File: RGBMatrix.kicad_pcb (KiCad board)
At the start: 2 copper layers, 208 parts

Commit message: anodColumn, colorRow
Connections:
- LED10 pad 1: B10 -> B01
- LED10 pad 2: G10 -> G01
- LED10 pad 3: R10 -> R01
- LED10 pad 4: A01 -> A10
- LED100 pad 1: B04 -> B07
- LED100 pad 2: G04 -> G07
- LED100 pad 3: R04 -> R07
- LED100 pad 4: A07 -> A04
- LED101 pad 1: B05 -> B07
- LED101 pad 2: G05 -> G07
- LED101 pad 3: R05 -> R07
- LED101 pad 4: A07 -> A05
- LED102 pad 1: B06 -> B07
- LED102 pad 2: G06 -> G07
- LED102 pad 3: R06 -> R07
- LED102 pad 4: A07 -> A06
- LED104 pad 1: B08 -> B07
- LED104 pad 2: G08 -> G07
- LED104 pad 3: R08 -> R07
- LED104 pad 4: A07 -> A08
- LED105 pad 1: B09 -> B07
- LED105 pad 2: G09 -> G07
- LED105 pad 3: R09 -> R07
- LED105 pad 4: A07 -> A09
- LED106 pad 1: B10 -> B07
- LED106 pad 2: G10 -> G07
- LED106 pad 3: R10 -> R07
- LED106 pad 4: A07 -> A10
- LED107 pad 1: B11 -> B07
- LED107 pad 2: G11 -> G07
- LED107 pad 3: R11 -> R07
- LED107 pad 4: A07 -> A11
- LED108 pad 1: B12 -> B07
- LED108 pad 2: G12 -> G07
- LED108 pad 3: R12 -> R07
- LED108 pad 4: A07 -> A12
- LED109 pad 1: B13 -> B07
- LED109 pad 2: G13 -> G07
- LED109 pad 3: R13 -> R07
- LED109 pad 4: A07 -> A13
- LED11 pad 1: B11 -> B01
- LED11 pad 2: G11 -> G01
- LED11 pad 3: R11 -> R01
- LED11 pad 4: A01 -> A11
- LED110 pad 1: B14 -> B07
- LED110 pad 2: G14 -> G07
- LED110 pad 3: R14 -> R07
- LED110 pad 4: A07 -> A14
- LED111 pad 1: B15 -> B07
- LED111 pad 2: G15 -> G07
- LED111 pad 3: R15 -> R07
- LED111 pad 4: A07 -> A15
- LED112 pad 1: B16 -> B07
- LED112 pad 2: G16 -> G07
- LED112 pad 3: R16 -> R07
- LED112 pad 4: A07 -> A16
- LED113 pad 1: B01 -> B08
- LED113 pad 2: G01 -> G08
- LED113 pad 3: R01 -> R08
- LED113 pad 4: A08 -> A01
- LED114 pad 1: B02 -> B08
- LED114 pad 2: G02 -> G08
- LED114 pad 3: R02 -> R08
- LED114 pad 4: A08 -> A02
- LED115 pad 1: B03 -> B08
- LED115 pad 2: G03 -> G08
- LED115 pad 3: R03 -> R08
- LED115 pad 4: A08 -> A03
- LED116 pad 1: B04 -> B08
- LED116 pad 2: G04 -> G08
- LED116 pad 3: R04 -> R08
- LED116 pad 4: A08 -> A04
- LED117 pad 1: B05 -> B08
- LED117 pad 2: G05 -> G08
- LED117 pad 3: R05 -> R08
- LED117 pad 4: A08 -> A05
- LED118 pad 1: B06 -> B08
- LED118 pad 2: G06 -> G08
- LED118 pad 3: R06 -> R08
- LED118 pad 4: A08 -> A06
- LED119 pad 1: B07 -> B08
- LED119 pad 2: G07 -> G08
- LED119 pad 3: R07 -> R08
- LED119 pad 4: A08 -> A07
- LED12 pad 1: B12 -> B01
- LED12 pad 2: G12 -> G01
- LED12 pad 3: R12 -> R01
- LED12 pad 4: A01 -> A12
- LED121 pad 1: B09 -> B08
- LED121 pad 2: G09 -> G08
- LED121 pad 3: R09 -> R08
- LED121 pad 4: A08 -> A09
- LED122 pad 1: B10 -> B08
- LED122 pad 2: G10 -> G08
- LED122 pad 3: R10 -> R08
- LED122 pad 4: A08 -> A10
- LED123 pad 1: B11 -> B08
- LED123 pad 2: G11 -> G08
- LED123 pad 3: R11 -> R08
- LED123 pad 4: A08 -> A11
- LED124 pad 1: B12 -> B08
- LED124 pad 2: G12 -> G08
- LED124 pad 3: R12 -> R08
- LED124 pad 4: A08 -> A12
- LED125 pad 1: B13 -> B08
- LED125 pad 2: G13 -> G08
- LED125 pad 3: R13 -> R08
- LED125 pad 4: A08 -> A13
- LED126 pad 1: B14 -> B08
- LED126 pad 2: G14 -> G08
- LED126 pad 3: R14 -> R08
- LED126 pad 4: A08 -> A14
- LED127 pad 1: B15 -> B08
- LED127 pad 2: G15 -> G08
- LED127 pad 3: R15 -> R08
- LED127 pad 4: A08 -> A15
- LED128 pad 1: B16 -> B08
- LED128 pad 2: G16 -> G08
- LED128 pad 3: R16 -> R08
- LED128 pad 4: A08 -> A16
- LED129 pad 1: B01 -> B09
- LED129 pad 2: G01 -> G09
- LED129 pad 3: R01 -> R09
- LED129 pad 4: A09 -> A01
- LED13 pad 1: B13 -> B01
- LED13 pad 2: G13 -> G01
- LED13 pad 3: R13 -> R01
- LED13 pad 4: A01 -> A13
- LED130 pad 1: B02 -> B09
- LED130 pad 2: G02 -> G09
- LED130 pad 3: R02 -> R09
- LED130 pad 4: A09 -> A02
- LED131 pad 1: B03 -> B09
- LED131 pad 2: G03 -> G09
- LED131 pad 3: R03 -> R09
- LED131 pad 4: A09 -> A03
- LED132 pad 1: B04 -> B09
- LED132 pad 2: G04 -> G09
- LED132 pad 3: R04 -> R09
- LED132 pad 4: A09 -> A04
- LED133 pad 1: B05 -> B09
- LED133 pad 2: G05 -> G09
- LED133 pad 3: R05 -> R09
- LED133 pad 4: A09 -> A05
- LED134 pad 1: B06 -> B09
- LED134 pad 2: G06 -> G09
- LED134 pad 3: R06 -> R09
- LED134 pad 4: A09 -> A06
- LED135 pad 1: B07 -> B09
- LED135 pad 2: G07 -> G09
- LED135 pad 3: R07 -> R09
- LED135 pad 4: A09 -> A07
- LED136 pad 1: B08 -> B09
- LED136 pad 2: G08 -> G09
- LED136 pad 3: R08 -> R09
- LED136 pad 4: A09 -> A08
- LED138 pad 1: B10 -> B09
- LED138 pad 2: G10 -> G09
- LED138 pad 3: R10 -> R09
- LED138 pad 4: A09 -> A10
- LED139 pad 1: B11 -> B09
- LED139 pad 2: G11 -> G09
- LED139 pad 3: R11 -> R09
- LED139 pad 4: A09 -> A11
- LED14 pad 1: B14 -> B01
- LED14 pad 2: G14 -> G01
- LED14 pad 3: R14 -> R01
- LED14 pad 4: A01 -> A14
- LED140 pad 1: B12 -> B09
- LED140 pad 2: G12 -> G09
- LED140 pad 3: R12 -> R09
- LED140 pad 4: A09 -> A12
- LED141 pad 1: B13 -> B09
- LED141 pad 2: G13 -> G09
- LED141 pad 3: R13 -> R09
- LED141 pad 4: A09 -> A13
- LED142 pad 1: B14 -> B09
- LED142 pad 2: G14 -> G09
- LED142 pad 3: R14 -> R09
- LED142 pad 4: A09 -> A14
- LED143 pad 1: B15 -> B09
- LED143 pad 2: G15 -> G09
- LED143 pad 3: R15 -> R09
- LED143 pad 4: A09 -> A15
- LED144 pad 1: B16 -> B09
- LED144 pad 2: G16 -> G09
- LED144 pad 3: R16 -> R09
- LED144 pad 4: A09 -> A16
- LED145 pad 1: B01 -> B10
- LED145 pad 2: G01 -> G10
- LED145 pad 3: R01 -> R10
- LED145 pad 4: A10 -> A01
- LED146 pad 1: B02 -> B10
- LED146 pad 2: G02 -> G10
- LED146 pad 3: R02 -> R10
- LED146 pad 4: A10 -> A02
- LED147 pad 1: B03 -> B10
- LED147 pad 2: G03 -> G10
- LED147 pad 3: R03 -> R10
- LED147 pad 4: A10 -> A03
- LED148 pad 1: B04 -> B10
- LED148 pad 2: G04 -> G10
- LED148 pad 3: R04 -> R10
- LED148 pad 4: A10 -> A04
- LED149 pad 1: B05 -> B10
- LED149 pad 2: G05 -> G10
- LED149 pad 3: R05 -> R10
- LED149 pad 4: A10 -> A05
- LED15 pad 1: B15 -> B01
- LED15 pad 2: G15 -> G01
- LED15 pad 3: R15 -> R01
- LED15 pad 4: A01 -> A15
- LED150 pad 1: B06 -> B10
- LED150 pad 2: G06 -> G10
- LED150 pad 3: R06 -> R10
- LED150 pad 4: A10 -> A06
- LED151 pad 1: B07 -> B10
- LED151 pad 2: G07 -> G10
- LED151 pad 3: R07 -> R10
- LED151 pad 4: A10 -> A07
- LED152 pad 1: B08 -> B10
- LED152 pad 2: G08 -> G10
- LED152 pad 3: R08 -> R10
- LED152 pad 4: A10 -> A08
- LED153 pad 1: B09 -> B10
- LED153 pad 2: G09 -> G10
- LED153 pad 3: R09 -> R10
- LED153 pad 4: A10 -> A09
- LED155 pad 1: B11 -> B10
- LED155 pad 2: G11 -> G10
- LED155 pad 3: R11 -> R10
- LED155 pad 4: A10 -> A11
- LED156 pad 1: B12 -> B10
- LED156 pad 2: G12 -> G10
- LED156 pad 3: R12 -> R10
- LED156 pad 4: A10 -> A12
- LED157 pad 1: B13 -> B10
- LED157 pad 2: G13 -> G10
- LED157 pad 3: R13 -> R10
- LED157 pad 4: A10 -> A13
- LED158 pad 1: B14 -> B10
- LED158 pad 2: G14 -> G10
- LED158 pad 3: R14 -> R10
- LED158 pad 4: A10 -> A14
- LED159 pad 1: B15 -> B10
- LED159 pad 2: G15 -> G10
- LED159 pad 3: R15 -> R10
- LED159 pad 4: A10 -> A15
- LED16 pad 1: B16 -> B01
- LED16 pad 2: G16 -> G01
- LED16 pad 3: R16 -> R01
- LED16 pad 4: A01 -> A16
- LED160 pad 1: B16 -> B10
- LED160 pad 2: G16 -> G10
- LED160 pad 3: R16 -> R10
- LED160 pad 4: A10 -> A16
- LED161 pad 1: B01 -> B11
- LED161 pad 2: G01 -> G11
- LED161 pad 3: R01 -> R11
- LED161 pad 4: A11 -> A01
- LED162 pad 1: B02 -> B11
- LED162 pad 2: G02 -> G11
- LED162 pad 3: R02 -> R11
- LED162 pad 4: A11 -> A02
- LED163 pad 1: B03 -> B11
- LED163 pad 2: G03 -> G11
- LED163 pad 3: R03 -> R11
- LED163 pad 4: A11 -> A03
- LED164 pad 1: B04 -> B11
- LED164 pad 2: G04 -> G11
- LED164 pad 3: R04 -> R11
- LED164 pad 4: A11 -> A04
- LED165 pad 1: B05 -> B11
- LED165 pad 2: G05 -> G11
- LED165 pad 3: R05 -> R11
- LED165 pad 4: A11 -> A05
- LED166 pad 1: B06 -> B11
- LED166 pad 2: G06 -> G11
- LED166 pad 3: R06 -> R11
- LED166 pad 4: A11 -> A06
- LED167 pad 1: B07 -> B11
- LED167 pad 2: G07 -> G11
- LED167 pad 3: R07 -> R11
- LED167 pad 4: A11 -> A07
- LED168 pad 1: B08 -> B11
- LED168 pad 2: G08 -> G11
- LED168 pad 3: R08 -> R11
- LED168 pad 4: A11 -> A08
- LED169 pad 1: B09 -> B11
- LED169 pad 2: G09 -> G11
- LED169 pad 3: R09 -> R11
- LED169 pad 4: A11 -> A09
- LED17 pad 1: B01 -> B02
- LED17 pad 2: G01 -> G02
- LED17 pad 3: R01 -> R02
- LED17 pad 4: A02 -> A01
- LED170 pad 1: B10 -> B11
- LED170 pad 2: G10 -> G11
- LED170 pad 3: R10 -> R11
- LED170 pad 4: A11 -> A10
- LED172 pad 1: B12 -> B11
- LED172 pad 2: G12 -> G11
- LED172 pad 3: R12 -> R11
- LED172 pad 4: A11 -> A12
- LED173 pad 1: B13 -> B11
- LED173 pad 2: G13 -> G11
- LED173 pad 3: R13 -> R11
- LED173 pad 4: A11 -> A13
- LED174 pad 1: B14 -> B11
- LED174 pad 2: G14 -> G11
- LED174 pad 3: R14 -> R11
- LED174 pad 4: A11 -> A14
- LED175 pad 1: B15 -> B11
- LED175 pad 2: G15 -> G11
- LED175 pad 3: R15 -> R11
- LED175 pad 4: A11 -> A15
- LED176 pad 1: B16 -> B11
- LED176 pad 2: G16 -> G11
- LED176 pad 3: R16 -> R11
- LED176 pad 4: A11 -> A16
- LED177 pad 1: B01 -> B12
- LED177 pad 2: G01 -> G12
- LED177 pad 3: R01 -> R12
- LED177 pad 4: A12 -> A01
- LED178 pad 1: B02 -> B12
- LED178 pad 2: G02 -> G12
- LED178 pad 3: R02 -> R12
- LED178 pad 4: A12 -> A02
- LED179 pad 1: B03 -> B12
- LED179 pad 2: G03 -> G12
- LED179 pad 3: R03 -> R12
- LED179 pad 4: A12 -> A03
- LED180 pad 1: B04 -> B12
- LED180 pad 2: G04 -> G12
- LED180 pad 3: R04 -> R12
- LED180 pad 4: A12 -> A04
- LED181 pad 1: B05 -> B12
- LED181 pad 2: G05 -> G12
- LED181 pad 3: R05 -> R12
- LED181 pad 4: A12 -> A05
- LED182 pad 1: B06 -> B12
- LED182 pad 2: G06 -> G12
- LED182 pad 3: R06 -> R12
- LED182 pad 4: A12 -> A06
- LED183 pad 1: B07 -> B12
- LED183 pad 2: G07 -> G12
- LED183 pad 3: R07 -> R12
- LED183 pad 4: A12 -> A07
- LED184 pad 1: B08 -> B12
- LED184 pad 2: G08 -> G12
- LED184 pad 3: R08 -> R12
- LED184 pad 4: A12 -> A08
- LED185 pad 1: B09 -> B12
- LED185 pad 2: G09 -> G12
- LED185 pad 3: R09 -> R12
- LED185 pad 4: A12 -> A09
- LED186 pad 1: B10 -> B12
- LED186 pad 2: G10 -> G12
- LED186 pad 3: R10 -> R12
- LED186 pad 4: A12 -> A10
- LED187 pad 1: B11 -> B12
- LED187 pad 2: G11 -> G12
- LED187 pad 3: R11 -> R12
- LED187 pad 4: A12 -> A11
- LED189 pad 1: B13 -> B12
- LED189 pad 2: G13 -> G12
- LED189 pad 3: R13 -> R12
- LED189 pad 4: A12 -> A13
- LED19 pad 1: B03 -> B02
- LED19 pad 2: G03 -> G02
- LED19 pad 3: R03 -> R02
- LED19 pad 4: A02 -> A03
- LED190 pad 1: B14 -> B12
- LED190 pad 2: G14 -> G12
- LED190 pad 3: R14 -> R12
- LED190 pad 4: A12 -> A14
- LED191 pad 1: B15 -> B12
- LED191 pad 2: G15 -> G12
- LED191 pad 3: R15 -> R12
- LED191 pad 4: A12 -> A15
- LED192 pad 1: B16 -> B12
- LED192 pad 2: G16 -> G12
- LED192 pad 3: R16 -> R12
- LED192 pad 4: A12 -> A16
- LED193 pad 1: B01 -> B13
- LED193 pad 2: G01 -> G13
- LED193 pad 3: R01 -> R13
- LED193 pad 4: A13 -> A01
- LED194 pad 1: B02 -> B13
- LED194 pad 2: G02 -> G13
- LED194 pad 3: R02 -> R13
- LED194 pad 4: A13 -> A02
- LED195 pad 1: B03 -> B13
- LED195 pad 2: G03 -> G13
- LED195 pad 3: R03 -> R13
- LED195 pad 4: A13 -> A03
- LED196 pad 1: B04 -> B13
- LED196 pad 2: G04 -> G13
- LED196 pad 3: R04 -> R13
- LED196 pad 4: A13 -> A04
- LED197 pad 1: B05 -> B13
- LED197 pad 2: G05 -> G13
- LED197 pad 3: R05 -> R13
- LED197 pad 4: A13 -> A05
- LED198 pad 1: B06 -> B13
- LED198 pad 2: G06 -> G13
- LED198 pad 3: R06 -> R13
- LED198 pad 4: A13 -> A06
- LED199 pad 1: B07 -> B13
- LED199 pad 2: G07 -> G13
- LED199 pad 3: R07 -> R13
- LED199 pad 4: A13 -> A07
- LED2 pad 1: B02 -> B01
- LED2 pad 2: G02 -> G01
- LED2 pad 3: R02 -> R01
- LED2 pad 4: A01 -> A02
- LED20 pad 1: B04 -> B02
- LED20 pad 2: G04 -> G02
- LED20 pad 3: R04 -> R02
- LED20 pad 4: A02 -> A04
- LED200 pad 1: B08 -> B13
- LED200 pad 2: G08 -> G13
- LED200 pad 3: R08 -> R13
- LED200 pad 4: A13 -> A08
- LED201 pad 1: B09 -> B13
- LED201 pad 2: G09 -> G13
- LED201 pad 3: R09 -> R13
- LED201 pad 4: A13 -> A09
- LED202 pad 1: B10 -> B13
- LED202 pad 2: G10 -> G13
- LED202 pad 3: R10 -> R13
- LED202 pad 4: A13 -> A10
- LED203 pad 1: B11 -> B13
- LED203 pad 2: G11 -> G13
- LED203 pad 3: R11 -> R13
- LED203 pad 4: A13 -> A11
- LED204 pad 1: B12 -> B13
- LED204 pad 2: G12 -> G13
- LED204 pad 3: R12 -> R13
- LED204 pad 4: A13 -> A12
- LED206 pad 1: B14 -> B13
- LED206 pad 2: G14 -> G13
- LED206 pad 3: R14 -> R13
- LED206 pad 4: A13 -> A14
- LED207 pad 1: B15 -> B13
- LED207 pad 2: G15 -> G13
- LED207 pad 3: R15 -> R13
- LED207 pad 4: A13 -> A15
- LED208 pad 1: B16 -> B13
- LED208 pad 2: G16 -> G13
- LED208 pad 3: R16 -> R13
- LED208 pad 4: A13 -> A16
- LED21 pad 1: B05 -> B02
- LED21 pad 2: G05 -> G02
- LED21 pad 3: R05 -> R02
- LED21 pad 4: A02 -> A05
- LED22 pad 1: B06 -> B02
- LED22 pad 2: G06 -> G02
- LED22 pad 3: R06 -> R02
- LED22 pad 4: A02 -> A06
- LED23 pad 1: B07 -> B02
- LED23 pad 2: G07 -> G02
- LED23 pad 3: R07 -> R02
- LED23 pad 4: A02 -> A07
- LED24 pad 1: B08 -> B02
- LED24 pad 2: G08 -> G02
- LED24 pad 3: R08 -> R02
- LED24 pad 4: A02 -> A08
- LED25 pad 1: B09 -> B02
- LED25 pad 2: G09 -> G02
- LED25 pad 3: R09 -> R02
- LED25 pad 4: A02 -> A09
- LED26 pad 1: B10 -> B02
- LED26 pad 2: G10 -> G02
- LED26 pad 3: R10 -> R02
- LED26 pad 4: A02 -> A10
- LED27 pad 1: B11 -> B02
- LED27 pad 2: G11 -> G02
- LED27 pad 3: R11 -> R02
- LED27 pad 4: A02 -> A11
- LED28 pad 1: B12 -> B02
- LED28 pad 2: G12 -> G02
- LED28 pad 3: R12 -> R02
- LED28 pad 4: A02 -> A12
- LED29 pad 1: B13 -> B02
- LED29 pad 2: G13 -> G02
- LED29 pad 3: R13 -> R02
- LED29 pad 4: A02 -> A13
- LED3 pad 1: B03 -> B01
- LED3 pad 2: G03 -> G01
- LED3 pad 3: R03 -> R01
- LED3 pad 4: A01 -> A03
- LED30 pad 1: B14 -> B02
- LED30 pad 2: G14 -> G02
- LED30 pad 3: R14 -> R02
- LED30 pad 4: A02 -> A14
- LED31 pad 1: B15 -> B02
- LED31 pad 2: G15 -> G02
- LED31 pad 3: R15 -> R02
- LED31 pad 4: A02 -> A15
- LED32 pad 1: B16 -> B02
- LED32 pad 2: G16 -> G02
- LED32 pad 3: R16 -> R02
- LED32 pad 4: A02 -> A16
- LED33 pad 1: B01 -> B03
- LED33 pad 2: G01 -> G03
- LED33 pad 3: R01 -> R03
- LED33 pad 4: A03 -> A01
- LED34 pad 1: B02 -> B03
- LED34 pad 2: G02 -> G03
- LED34 pad 3: R02 -> R03
- LED34 pad 4: A03 -> A02
- LED36 pad 1: B04 -> B03
- LED36 pad 2: G04 -> G03
- LED36 pad 3: R04 -> R03
- LED36 pad 4: A03 -> A04
- LED37 pad 1: B05 -> B03
- LED37 pad 2: G05 -> G03
- LED37 pad 3: R05 -> R03
- LED37 pad 4: A03 -> A05
- LED38 pad 1: B06 -> B03
- LED38 pad 2: G06 -> G03
- LED38 pad 3: R06 -> R03
- LED38 pad 4: A03 -> A06
- LED39 pad 1: B07 -> B03
- LED39 pad 2: G07 -> G03
- LED39 pad 3: R07 -> R03
- LED39 pad 4: A03 -> A07
- LED4 pad 1: B04 -> B01
- LED4 pad 2: G04 -> G01
- LED4 pad 3: R04 -> R01
- LED4 pad 4: A01 -> A04
- LED40 pad 1: B08 -> B03
- LED40 pad 2: G08 -> G03
- LED40 pad 3: R08 -> R03
- LED40 pad 4: A03 -> A08
- LED41 pad 1: B09 -> B03
- LED41 pad 2: G09 -> G03
- LED41 pad 3: R09 -> R03
- LED41 pad 4: A03 -> A09
- LED42 pad 1: B10 -> B03
- LED42 pad 2: G10 -> G03
- LED42 pad 3: R10 -> R03
- LED42 pad 4: A03 -> A10
- LED43 pad 1: B11 -> B03
- LED43 pad 2: G11 -> G03
- LED43 pad 3: R11 -> R03
- LED43 pad 4: A03 -> A11
- LED44 pad 1: B12 -> B03
- LED44 pad 2: G12 -> G03
- LED44 pad 3: R12 -> R03
- LED44 pad 4: A03 -> A12
- LED45 pad 1: B13 -> B03
- LED45 pad 2: G13 -> G03
- LED45 pad 3: R13 -> R03
- LED45 pad 4: A03 -> A13
- LED46 pad 1: B14 -> B03
- LED46 pad 2: G14 -> G03
- LED46 pad 3: R14 -> R03
- LED46 pad 4: A03 -> A14
- LED47 pad 1: B15 -> B03
- LED47 pad 2: G15 -> G03
- LED47 pad 3: R15 -> R03
- LED47 pad 4: A03 -> A15
- LED48 pad 1: B16 -> B03
- LED48 pad 2: G16 -> G03
- LED48 pad 3: R16 -> R03
- LED48 pad 4: A03 -> A16
- LED49 pad 1: B01 -> B04
- LED49 pad 2: G01 -> G04
- LED49 pad 3: R01 -> R04
- LED49 pad 4: A04 -> A01
- LED5 pad 1: B05 -> B01
- LED5 pad 2: G05 -> G01
- LED5 pad 3: R05 -> R01
- LED5 pad 4: A01 -> A05
- LED50 pad 1: B02 -> B04
- LED50 pad 2: G02 -> G04
- LED50 pad 3: R02 -> R04
- LED50 pad 4: A04 -> A02
- LED51 pad 1: B03 -> B04
- LED51 pad 2: G03 -> G04
- LED51 pad 3: R03 -> R04
- LED51 pad 4: A04 -> A03
- LED53 pad 1: B05 -> B04
- LED53 pad 2: G05 -> G04
- LED53 pad 3: R05 -> R04
- LED53 pad 4: A04 -> A05
- LED54 pad 1: B06 -> B04
- LED54 pad 2: G06 -> G04
- LED54 pad 3: R06 -> R04
- LED54 pad 4: A04 -> A06
- LED55 pad 1: B07 -> B04
- LED55 pad 2: G07 -> G04
- LED55 pad 3: R07 -> R04
- LED55 pad 4: A04 -> A07
- LED56 pad 1: B08 -> B04
- LED56 pad 2: G08 -> G04
- LED56 pad 3: R08 -> R04
- LED56 pad 4: A04 -> A08
- LED57 pad 1: B09 -> B04
- LED57 pad 2: G09 -> G04
- LED57 pad 3: R09 -> R04
- LED57 pad 4: A04 -> A09
- LED58 pad 1: B10 -> B04
- LED58 pad 2: G10 -> G04
- LED58 pad 3: R10 -> R04
- LED58 pad 4: A04 -> A10
- LED59 pad 1: B11 -> B04
- LED59 pad 2: G11 -> G04
- LED59 pad 3: R11 -> R04
- LED59 pad 4: A04 -> A11
- LED6 pad 1: B06 -> B01
- LED6 pad 2: G06 -> G01
- LED6 pad 3: R06 -> R01
- LED6 pad 4: A01 -> A06
- LED60 pad 1: B12 -> B04
- LED60 pad 2: G12 -> G04
- LED60 pad 3: R12 -> R04
- LED60 pad 4: A04 -> A12
- LED61 pad 1: B13 -> B04
- LED61 pad 2: G13 -> G04
- LED61 pad 3: R13 -> R04
- LED61 pad 4: A04 -> A13
- LED62 pad 1: B14 -> B04
- LED62 pad 2: G14 -> G04
- LED62 pad 3: R14 -> R04
- LED62 pad 4: A04 -> A14
- LED63 pad 1: B15 -> B04
- LED63 pad 2: G15 -> G04
- LED63 pad 3: R15 -> R04
- LED63 pad 4: A04 -> A15
- LED64 pad 1: B16 -> B04
- LED64 pad 2: G16 -> G04
- LED64 pad 3: R16 -> R04
- LED64 pad 4: A04 -> A16
- LED65 pad 1: B01 -> B05
- LED65 pad 2: G01 -> G05
- LED65 pad 3: R01 -> R05
- LED65 pad 4: A05 -> A01
- LED66 pad 1: B02 -> B05
- LED66 pad 2: G02 -> G05
- LED66 pad 3: R02 -> R05
- LED66 pad 4: A05 -> A02
- LED67 pad 1: B03 -> B05
- LED67 pad 2: G03 -> G05
- LED67 pad 3: R03 -> R05
- LED67 pad 4: A05 -> A03
- LED68 pad 1: B04 -> B05
- LED68 pad 2: G04 -> G05
- LED68 pad 3: R04 -> R05
- LED68 pad 4: A05 -> A04
- LED7 pad 1: B07 -> B01
- LED7 pad 2: G07 -> G01
- LED7 pad 3: R07 -> R01
- LED7 pad 4: A01 -> A07
- LED70 pad 1: B06 -> B05
- LED70 pad 2: G06 -> G05
- LED70 pad 3: R06 -> R05
- LED70 pad 4: A05 -> A06
- LED71 pad 1: B07 -> B05
- LED71 pad 2: G07 -> G05
- LED71 pad 3: R07 -> R05
- LED71 pad 4: A05 -> A07
- LED72 pad 1: B08 -> B05
- LED72 pad 2: G08 -> G05
- LED72 pad 3: R08 -> R05
- LED72 pad 4: A05 -> A08
- LED73 pad 1: B09 -> B05
- LED73 pad 2: G09 -> G05
- LED73 pad 3: R09 -> R05
- LED73 pad 4: A05 -> A09
- LED74 pad 1: B10 -> B05
- LED74 pad 2: G10 -> G05
- LED74 pad 3: R10 -> R05
- LED74 pad 4: A05 -> A10
- LED75 pad 1: B11 -> B05
- LED75 pad 2: G11 -> G05
- LED75 pad 3: R11 -> R05
- LED75 pad 4: A05 -> A11
- LED76 pad 1: B12 -> B05
- LED76 pad 2: G12 -> G05
- LED76 pad 3: R12 -> R05
- LED76 pad 4: A05 -> A12
- LED77 pad 1: B13 -> B05
- LED77 pad 2: G13 -> G05
- LED77 pad 3: R13 -> R05
- LED77 pad 4: A05 -> A13
- LED78 pad 1: B14 -> B05
- LED78 pad 2: G14 -> G05
- LED78 pad 3: R14 -> R05
- LED78 pad 4: A05 -> A14
- LED79 pad 1: B15 -> B05
- LED79 pad 2: G15 -> G05
- LED79 pad 3: R15 -> R05
- LED79 pad 4: A05 -> A15
- LED8 pad 1: B08 -> B01
- LED8 pad 2: G08 -> G01
- LED8 pad 3: R08 -> R01
- LED8 pad 4: A01 -> A08
- LED80 pad 1: B16 -> B05
- LED80 pad 2: G16 -> G05
- LED80 pad 3: R16 -> R05
- LED80 pad 4: A05 -> A16
- LED81 pad 1: B01 -> B06
- LED81 pad 2: G01 -> G06
- LED81 pad 3: R01 -> R06
- LED81 pad 4: A06 -> A01
- LED82 pad 1: B02 -> B06
- LED82 pad 2: G02 -> G06
- LED82 pad 3: R02 -> R06
- LED82 pad 4: A06 -> A02
- LED83 pad 1: B03 -> B06
- LED83 pad 2: G03 -> G06
- LED83 pad 3: R03 -> R06
- LED83 pad 4: A06 -> A03
- LED84 pad 1: B04 -> B06
- LED84 pad 2: G04 -> G06
- LED84 pad 3: R04 -> R06
- LED84 pad 4: A06 -> A04
- LED85 pad 1: B05 -> B06
- LED85 pad 2: G05 -> G06
- LED85 pad 3: R05 -> R06
- LED85 pad 4: A06 -> A05
- LED87 pad 1: B07 -> B06
- LED87 pad 2: G07 -> G06
- LED87 pad 3: R07 -> R06
- LED87 pad 4: A06 -> A07
- LED88 pad 1: B08 -> B06
- LED88 pad 2: G08 -> G06
- LED88 pad 3: R08 -> R06
- LED88 pad 4: A06 -> A08
- LED89 pad 1: B09 -> B06
- LED89 pad 2: G09 -> G06
- LED89 pad 3: R09 -> R06
- LED89 pad 4: A06 -> A09
- LED9 pad 1: B09 -> B01
- LED9 pad 2: G09 -> G01
- LED9 pad 3: R09 -> R01
- LED9 pad 4: A01 -> A09
- LED90 pad 1: B10 -> B06
- LED90 pad 2: G10 -> G06
- LED90 pad 3: R10 -> R06
- LED90 pad 4: A06 -> A10
- LED91 pad 1: B11 -> B06
- LED91 pad 2: G11 -> G06
- LED91 pad 3: R11 -> R06
- LED91 pad 4: A06 -> A11
- LED92 pad 1: B12 -> B06
- LED92 pad 2: G12 -> G06
- LED92 pad 3: R12 -> R06
- LED92 pad 4: A06 -> A12
- LED93 pad 1: B13 -> B06
- LED93 pad 2: G13 -> G06
- LED93 pad 3: R13 -> R06
- LED93 pad 4: A06 -> A13
- LED94 pad 1: B14 -> B06
- LED94 pad 2: G14 -> G06
- LED94 pad 3: R14 -> R06
- LED94 pad 4: A06 -> A14
- LED95 pad 1: B15 -> B06
- LED95 pad 2: G15 -> G06
- LED95 pad 3: R15 -> R06
- LED95 pad 4: A06 -> A15
- LED96 pad 1: B16 -> B06
- LED96 pad 2: G16 -> G06
- LED96 pad 3: R16 -> R06
- LED96 pad 4: A06 -> A16
- LED97 pad 1: B01 -> B07
- LED97 pad 2: G01 -> G07
- LED97 pad 3: R01 -> R07
- LED97 pad 4: A07 -> A01
- LED98 pad 1: B02 -> B07
- LED98 pad 2: G02 -> G07
- LED98 pad 3: R02 -> R07
- LED98 pad 4: A07 -> A02
- LED99 pad 1: B03 -> B07
- LED99 pad 2: G03 -> G07
- LED99 pad 3: R03 -> R07
- LED99 pad 4: A07 -> A03
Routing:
- net A16: track 0.00 -> 27.6 mm, vias 0 -> 13
- net A15: track 0.00 -> 27.6 mm, vias 0 -> 13
- net A14: track 0.00 -> 27.6 mm, vias 0 -> 13
- net A13: track 0.00 -> 27.6 mm, vias 0 -> 13
- net A12: track 0.00 -> 27.6 mm, vias 0 -> 13
- net A11: track 0.00 -> 27.6 mm, vias 0 -> 13
- net A10: track 0.00 -> 27.6 mm, vias 0 -> 13
- net A09: track 0.00 -> 27.6 mm, vias 0 -> 13
- net A08: track 0.00 -> 27.6 mm, vias 0 -> 13
- net A07: track 0.00 -> 27.6 mm, vias 0 -> 13
- net A06: track 0.00 -> 27.6 mm, vias 0 -> 13
- net A05: track 0.00 -> 27.6 mm, vias 0 -> 13
- net A04: track 0.00 -> 27.6 mm, vias 0 -> 13
- net A03: track 0.00 -> 27.6 mm, vias 0 -> 13
- net A02: track 0.00 -> 27.6 mm, vias 0 -> 13
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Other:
- copper layers 2 -> 8

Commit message: update
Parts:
- added Q17: PNP, Package_TO_SOT_SMD:SOT-323_SC-70, B.Cu at (43.7, 87.0)
- added Q18: PNP, Package_TO_SOT_SMD:SOT-323_SC-70, B.Cu at (43.7, 90.4)
- added Q19: PNP, Package_TO_SOT_SMD:SOT-323_SC-70, B.Cu at (46.3, 87.0)
- added Q20: PNP, Package_TO_SOT_SMD:SOT-323_SC-70, B.Cu at (46.4, 90.4)
- added Q21: PNP, Package_TO_SOT_SMD:SOT-323_SC-70, B.Cu at (48.9, 87.0)
- added Q22: PNP, Package_TO_SOT_SMD:SOT-323_SC-70, B.Cu at (49.0, 90.4)
- added Q23: PNP, Package_TO_SOT_SMD:SOT-323_SC-70, B.Cu at (51.5, 87.0)
- added Q24: PNP, Package_TO_SOT_SMD:SOT-323_SC-70, B.Cu at (51.6, 90.4)
- added Q25: PNP, Package_TO_SOT_SMD:SOT-323_SC-70, B.Cu at (54.1, 87.0)
- added Q26: PNP, Package_TO_SOT_SMD:SOT-323_SC-70, B.Cu at (54.2, 90.4)
- added Q27: PNP, Package_TO_SOT_SMD:SOT-323_SC-70, B.Cu at (56.7, 87.0)
- added Q28: PNP, Package_TO_SOT_SMD:SOT-323_SC-70, B.Cu at (56.8, 90.4)
- added Q29: PNP, Package_TO_SOT_SMD:SOT-323_SC-70, B.Cu at (59.3, 87.0)
- added Q30: PNP, Package_TO_SOT_SMD:SOT-323_SC-70, B.Cu at (59.4, 90.4)
- added Q31: PNP, Package_TO_SOT_SMD:SOT-323_SC-70, B.Cu at (62.0, 87.0)
- added Q32: PNP, Package_TO_SOT_SMD:SOT-323_SC-70, B.Cu at (62.0, 90.4)
- added RN1: R_Pack08, Resistor_SMD:R_Array_Convex_8x0602, B.Cu at (46.5, 64.7)
- added RN2: R_Pack08, Resistor_SMD:R_Array_Convex_8x0602, B.Cu at (46.5, 70.2)
- added RN3: R_Pack08, Resistor_SMD:R_Array_Convex_8x0602, B.Cu at (57.6, 53.6)
- added RN4: R_Pack08, Resistor_SMD:R_Array_Convex_8x0602, B.Cu at (57.6, 59.1)
- added RN5: R_Pack08, Resistor_SMD:R_Array_Convex_8x0602, B.Cu at (52.0, 83.5)
- added RN6: R_Pack08, Resistor_SMD:R_Array_Convex_8x0602, B.Cu at (46.5, 83.5)
- added RN7: R_Pack08, Resistor_SMD:R_Array_Convex_8x0602, B.Cu at (60.2, 83.5)
- added RN8: R_Pack08, Resistor_SMD:R_Array_Convex_8x0602, B.Cu at (58.3, 72.0)
- added U1: 74LS596, Package_SO:TSSOP-16_4.4x5mm_P0.65mm, B.Cu at (52.1, 64.7)
- added U2: 74LS596, Package_SO:TSSOP-16_4.4x5mm_P0.65mm, B.Cu at (52.1, 70.2)
- added U3: 74LS596, Package_SO:TSSOP-16_4.4x5mm_P0.65mm, B.Cu at (52.1, 53.6)
- added U4: 74LS596, Package_SO:TSSOP-16_4.4x5mm_P0.65mm, B.Cu at (52.1, 59.1)
- added U5: 74LS596, Package_SO:TSSOP-16_4.4x5mm_P0.65mm, B.Cu at (52.0, 78.0)
- added U6: 74LS596, Package_SO:TSSOP-16_4.4x5mm_P0.65mm, B.Cu at (46.4, 78.0)
- added U7: 74154, Package_SO:TSSOP-24_4.4x7.8mm_P0.65mm, B.Cu at (58.9, 78.0)
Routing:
- net +3.3V: track 0.00 -> 42.2 mm, vias 0 -> 7
- net _OE: track 0.00 -> 37.7 mm, vias 0 -> 2
- net _SRCLR: track 0.00 -> 36.8 mm
- net G01: track 20.9 -> 55.5 mm, vias 16 -> 17
- net RCLK: track 0.00 -> 33.4 mm, vias 0 -> 6
- net SRCLK: track 0.00 -> 33.3 mm, vias 0 -> 6
- net G02: track 20.9 -> 53.0 mm, vias 16 -> 17
- net COL02: track 0.00 -> 30.8 mm, vias 0 -> 2
- net COL06: track 0.00 -> 30.3 mm, vias 0 -> 2
- net G03: track 20.9 -> 50.5 mm, vias 16 -> 17
- net COL01: track 0.00 -> 29.3 mm, vias 0 -> 2
- net G04: track 20.9 -> 48.0 mm, vias 16 -> 17
- net COL04: track 0.00 -> 27.1 mm, vias 0 -> 2
- net COL03: track 0.00 -> 24.8 mm, vias 0 -> 2
- net G05: track 20.9 -> 45.5 mm, vias 16 -> 17
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- added copper zone on In6.Cu, net GND
- added copper zone on B.Cu, net V_LED
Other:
- board outline added: 23.5 x 50 mm
- board text added: "VESZTETTEM"

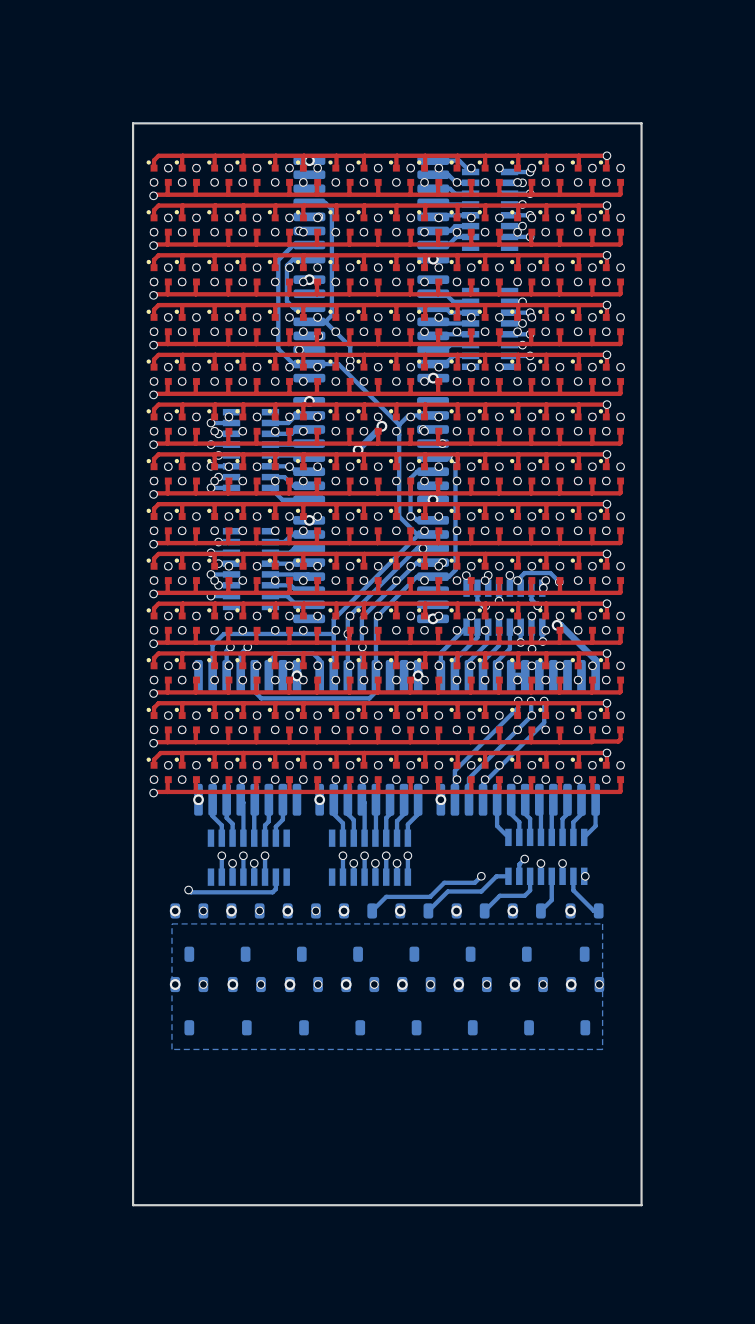
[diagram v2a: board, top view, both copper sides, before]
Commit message: progress
full wireing, ready for first check
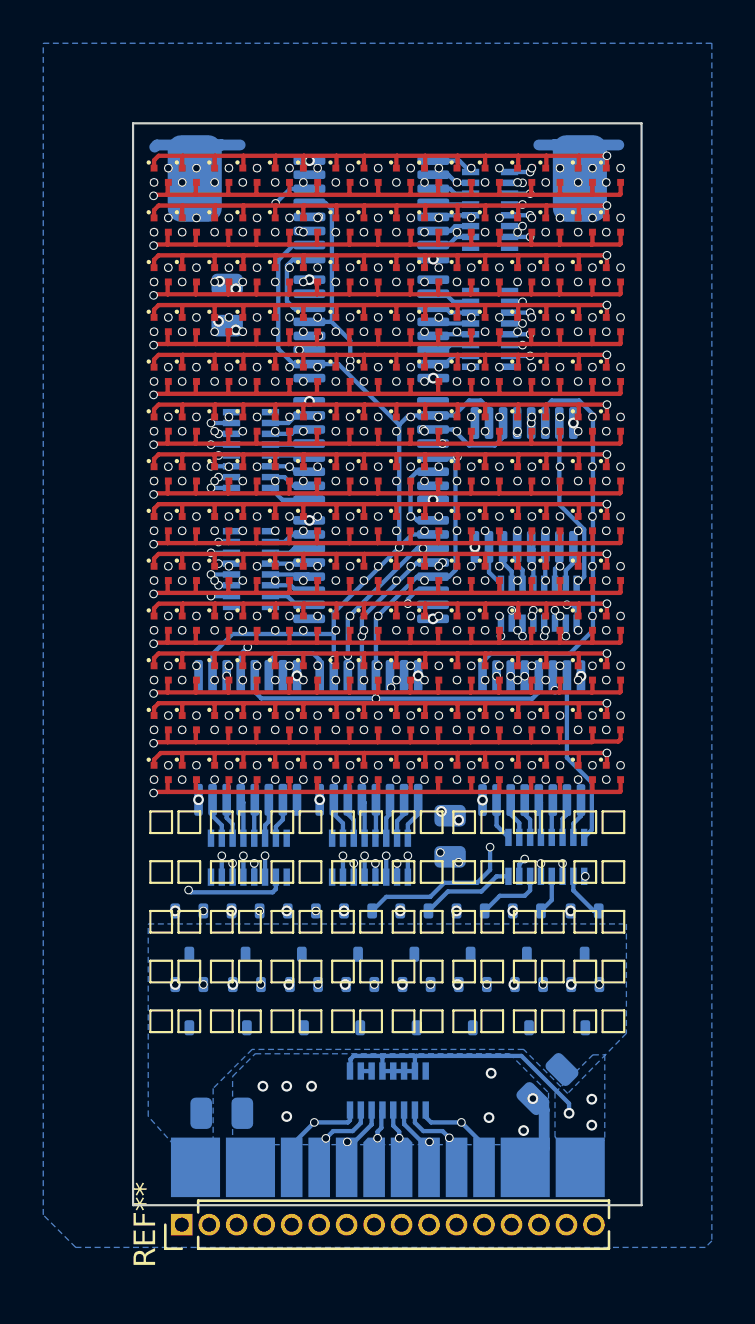
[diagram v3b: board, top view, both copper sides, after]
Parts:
- removed U7: 74154, Package_SO:TSSOP-24_4.4x7.8mm_P0.65mm
- added ?: , , F.Cu at (61.8, 52.1)
- added ?: , , F.Cu at (44.0, 52.1)
- added C1: C, Capacitor_SMD:C_0805_2012Metric, B.Cu at (45.2, 95.3)
- added C2: C, Capacitor_SMD:C_0805_2012Metric, B.Cu at (60.2, 94.0)
- added C3: C, Capacitor_SMD:C_0805_2012Metric, B.Cu at (45.5, 58.0)
- added C4: C, Capacitor_SMD:C_0805_2012Metric, B.Cu at (55.8, 82.5)
- added REF**: PinHeader_1x16_P1.27mm_Vertical, Connector_PinHeader_1.27mm:PinHeader_1x16_P1.27mm_Vertical, F.Cu at (43.4, 100.5)
- added RN9: R_Pack08, Resistor_SMD:R_Array_Convex_8x0602, B.Cu at (52.9, 94.3)
- added U8: 74LS596, Package_SO:TSSOP-16_4.4x5mm_P0.65mm, B.Cu at (59.5, 78.0)
- added U9: 74LS596, Package_SO:TSSOP-16_4.4x5mm_P0.65mm, B.Cu at (59.2, 66.3)
- moved RN8 1.60 mm to (59.9, 71.8), turned to -90 degrees
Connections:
- RN8 pad 10: COL04 -> COL07
- RN8 pad 11: COL03 -> COL06
- RN8 pad 12: COL02 -> COL05
- RN8 pad 13: COL01 -> COL04
- RN8 pad 14: COL06 -> COL03
- RN8 pad 15: COL07 -> COL02
- RN8 pad 16: COL08 -> COL01
- RN8 pad 9: COL05 -> COL08
- U1 pad 13: _OE -> _EN
- U2 pad 13: _OE -> _EN
- U3 pad 13: _OE -> _EN
- U4 pad 13: _OE -> _EN
- U5 pad 13: _OE -> _EN
- U6 pad 13: _OE -> _EN
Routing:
- net _EN: track 0.65 -> 77.2 mm, vias 0 -> 5
- net B_IN: track 0.00 -> 58.1 mm, vias 0 -> 2
- net RCLK: track 33.4 -> 78.5 mm, vias 6 -> 9
- net SRCLK: track 33.3 -> 77.4 mm, vias 6 -> 8
- net _SRCLR: track 36.8 -> 78.8 mm, vias 0 -> 4
- net _OE: track 37.7 -> 0.00 mm, vias 2 -> 0
- net R_IN: track 0.00 -> 35.1 mm, vias 0 -> 2
- net A_IN: track 0.00 -> 27.5 mm, vias 0 -> 2
- net G_IN: track 0.00 -> 26.8 mm, vias 0 -> 2
- net +3.3V: track 42.2 -> 18.9 mm, vias 7 -> 15
- net GND: track 1.56 -> 22.6 mm, vias 9 -> 20
- net Net-(U8-QH'): track 0.00 -> 19.7 mm
- net Net-(RN8-R3.1): track 9.24 -> 1.83 mm, vias 2 -> 0
- net Net-(RN8-R2.1): track 9.20 -> 1.89 mm, vias 2 -> 0
- net Net-(RN8-R1.1): track 9.19 -> 1.95 mm, vias 2 -> 0
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- added copper zone on B.Cu, net +3.3V
- added copper zone on In5.Cu, net +3.3V
- added copper zone on B.Cu, net GND
- added copper zone on In1.Cu, net GND
- added copper zone on In2.Cu, net GND
- added copper zone on In3.Cu, net GND
- added copper zone on In4.Cu, net GND
